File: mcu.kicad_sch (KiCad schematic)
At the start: 12 parts, among them U1 STM32G071C8Tx, Y1 NX3215SA-32.768K-STD-MUA-9

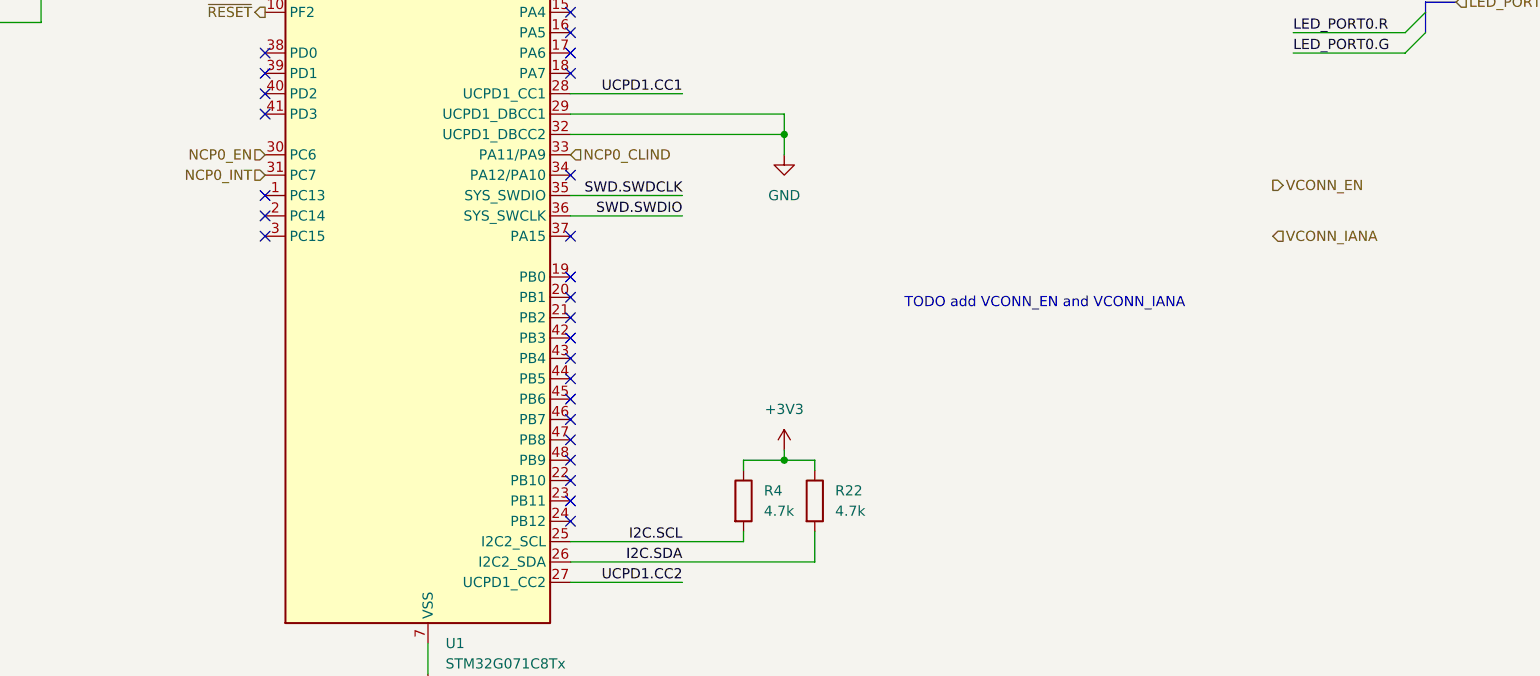
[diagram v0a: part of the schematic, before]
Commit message: Wire up vconn and analog pins
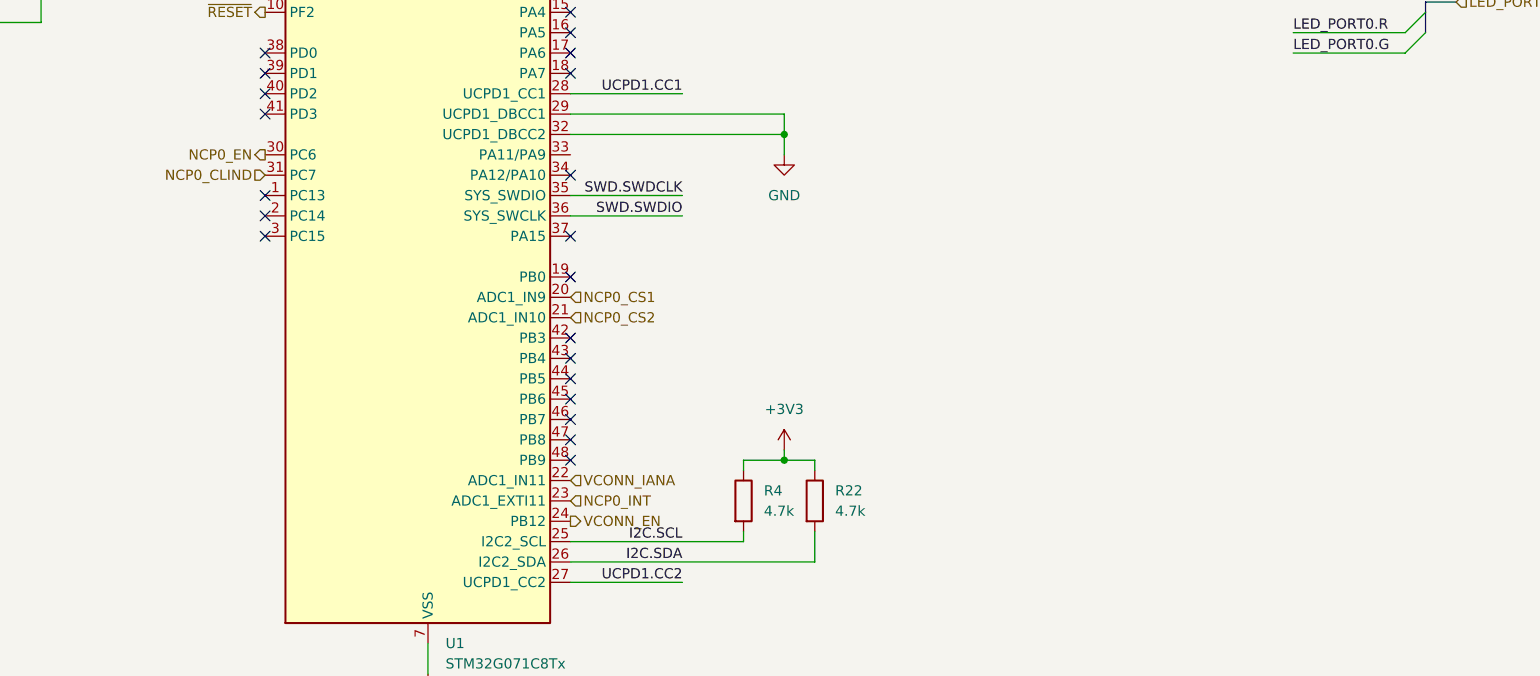
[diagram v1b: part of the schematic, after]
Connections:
- net NCP0_CLIND: now also U1.31 (PC7); no longer U1.33 (PA11/PA9)
- net NCP0_INT: now also U1.23 (PB11); no longer U1.31 (PC7)
- net VCONN_EN: now also U1.24 (PB12)
- net VCONN_IANA: now also U1.22 (PB10)
- net NCP0_CS1: now reaches U1.20 (PB1)
- net NCP0_CS2: now reaches U1.21 (PB2)
- no-connect marks 28 -> 23
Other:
- note removed: "TODO add VCONN_EN and VCONN_IANA"
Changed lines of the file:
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@@
-	)
-	(no_connect
-		(at 149.86 140.97)
-	)
-	(no_connect
-		(at 149.86 115.57)
 	)
 	(no_connect
@@
 	)
 	(no_connect
-		(at 149.86 138.43)
-	)
-	(no_connect
 		(at 149.86 74.93)
 	)
@@
 	)
 	(no_connect
-		(at 149.86 135.89)
-	)
-	(no_connect
 		(at 149.86 130.81)
 	)
@@
 	(no_connect
 		(at 149.86 105.41)
-	)
-	(no_connect
-		(at 149.86 113.03)
 	)
 	(bus_entry
@@
 		)
 	)
-	(text "TODO add VCONN_EN and VCONN_IANA"
-		(exclude_from_sim no)
-		(at 209.042 113.792 0)
-		(effects
-			(font
-				(size 1.27 1.27)
-			)
-		)
-	)
 	(text "- USB PD primer (TI): https://www.ti.com/lit/wp/slyy109b/slyy109b.pdf?ts=1711082549009\n"
 		(exclude_from_sim no)
@@
 	(hierarchical_label "VCONN_EN"
 		(shape output)
-		(at 237.49 99.06 0)
+		(at 149.86 140.97 0)
 		(fields_autoplaced yes)
 		(effects
@@
 	(hierarchical_label "NCP0_CLIND"
 		(shape input)
-		(at 149.86 95.25 0)
+		(at 111.76 97.79 180)
+		(fields_autoplaced yes)
+		(effects
+			(font
+				(size 1.27 1.27)
+			)
+			(justify right)
+		)
+	)
+	(hierarchical_label "NCP0_EN"
+		(shape output)
+		(at 111.76 95.25 180)
+		(fields_autoplaced yes)
+		(effects
+			(font
+				(size 1.27 1.27)
+			)
+			(justify right)
+		)
+	)
+	(hierarchical_label "NCP0_CS2"
+		(shape input)
+		(at 149.86 115.57 0)
 		(fields_autoplaced yes)
 		(effects
@@
 		)
 	)
-	(hierarchical_label "NCP0_EN"
+	(hierarchical_label "NCP0_CS1"
 		(shape input)
-		(at 111.76 95.25 180)
-		(fields_autoplaced yes)
-		(effects
-			(font
-				(size 1.27 1.27)
-			)
-			(justify right)
+		(at 149.86 113.03 0)
+		(fields_autoplaced yes)
+		(effects
+			(font
+				(size 1.27 1.27)
+			)
+			(justify left)
 		)
 	)
@@
 	(hierarchical_label "NCP0_INT"
 		(shape input)
-		(at 111.76 97.79 180)
-		(fields_autoplaced yes)
-		(effects
-			(font
-				(size 1.27 1.27)
-			)
-			(justify right)
+		(at 149.86 138.43 0)
+		(fields_autoplaced yes)
+		(effects
+			(font
+				(size 1.27 1.27)
+			)
+			(justify left)
 		)
 	)
 	(hierarchical_label "VCONN_IANA"
 		(shape input)
-		(at 237.49 105.41 0)
+		(at 149.86 135.89 0)
 		(fields_autoplaced yes)
 		(effects
@@
 		)
 		(pin "21"
+			(alternate "ADC1_IN10")
 		)
 		(pin "10"
@@
 		)
 		(pin "23"
+			(alternate "ADC1_EXTI11")
 		)
 		(pin "45"
@@
 		)
 		(pin "20"
+			(alternate "ADC1_IN9")
 		)
 		(pin "19"
 		)
 		(pin "22"
+			(alternate "ADC1_IN11")
 		)
 		(pin "33"
@@
 		)
 		(pin "24"
+			(alternate "PB12")
 		)
 		(pin "36"

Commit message: Wire up VCONN_FLGn
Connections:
- net NCP0_INT: now also U1.33 (PA11/PA9); no longer U1.23 (PB11)
- new net VCONN_FLGn: U1.23 (PB11)
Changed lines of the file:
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@@
+		)
+	)
+	(hierarchical_label "VCONN_FLGn"
+		(shape input)
+		(at 149.86 138.43 0)
+		(fields_autoplaced yes)
+		(effects
+			(font
+				(size 1.27 1.27)
+			)
+			(justify left)
 		)
 	)
@@
 	(hierarchical_label "NCP0_INT"
 		(shape input)
-		(at 149.86 138.43 0)
+		(at 149.86 95.25 0)
 		(fields_autoplaced yes)
 		(effects

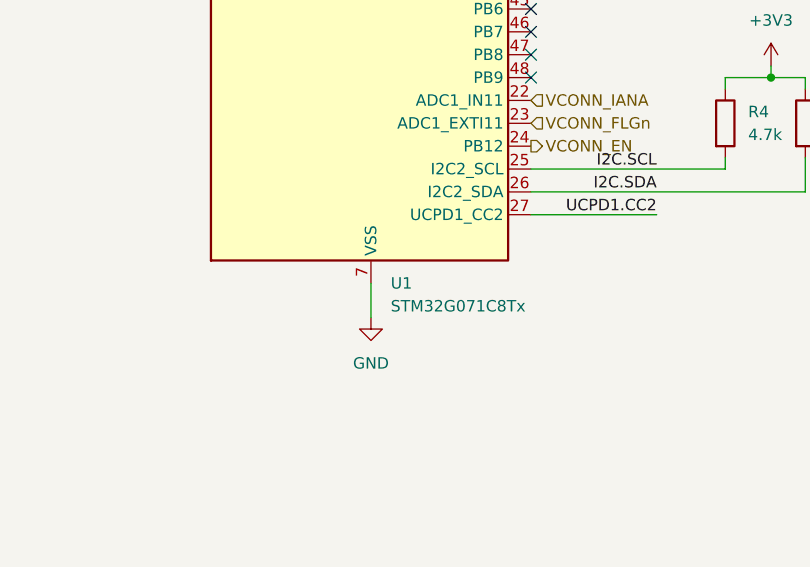
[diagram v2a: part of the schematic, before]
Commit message: Fix ERC errors, swap out mosfets for NVC chip
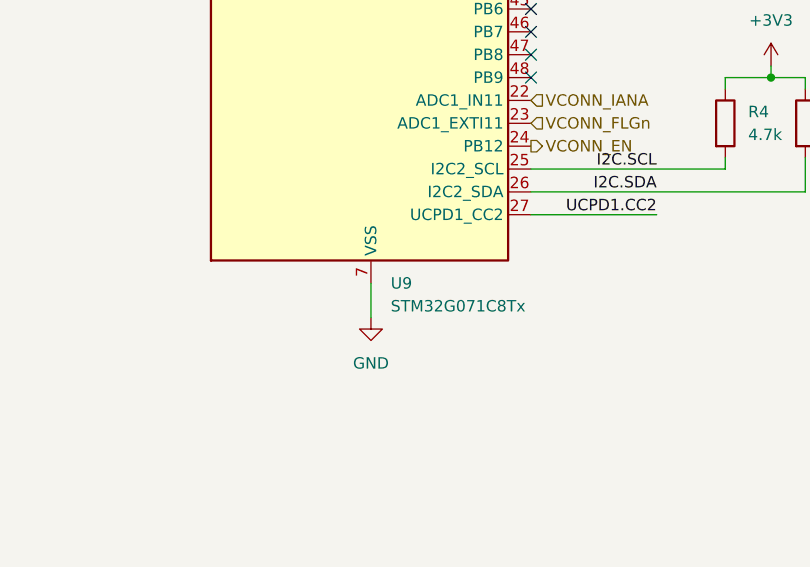
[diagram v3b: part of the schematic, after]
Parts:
- removed U1: STM32G071C8Tx, Package_QFP:LQFP-48_7x7mm_P0.5mm, symbol MCU_ST_STM32G0:STM32G071C8Tx
- added U9: STM32G071C8Tx, Package_QFP:LQFP-48_7x7mm_P0.5mm, symbol MCU_ST_STM32G0:STM32G071C8Tx
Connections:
- net +3V3: now also U9.4 (VBAT), U9.5 (VREF+), U9.6 (VDD)
- net GND: now also U9.29 (PA9/UCPD1_DBCC1), U9.32 (PA10/UCPD1_DBCC2), U9.7 (VSS)
- net I2C.SCL: now also U9.25 (PB13)
- net I2C.SDA: now also U9.26 (PB14)
- net LED_PORT0.G: now also U9.13 (PA2)
- net LED_PORT0.R: now also U9.12 (PA1)
- net NCP0_CLIND: now also U9.31 (PC7)
- net NCP0_CS1: now also U9.20 (PB1)
- net NCP0_CS2: now also U9.21 (PB2)
- net NCP0_EN: now also U9.30 (PC6)
- net NCP0_INT: now also U9.33 (PA11/PA9)
- net SWD.SWDCLK: now also U9.35 (PA13)
- net SWD.SWDIO: now also U9.36 (PA14)
- net UCPD1.CC1: now also U9.28 (PA8)
- net UCPD1.CC2: now also U9.27 (PB15)
- net VCONN_EN: now also U9.24 (PB12)
- net VCONN_FLGn: now also U9.23 (PB11)
- net VCONN_IANA: now also U9.22 (PB10)
- net ~{RESET}: now also U9.10 (PF2)
- net at C29.2, Y1.2: now also U9.8 (PF0)
- net at C30.2, Y1.1: now also U9.9 (PF1)
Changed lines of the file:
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@@
+	)
+	(symbol
+		(lib_name "STM32G071C8Tx_1")
+		(lib_id "MCU_ST_STM32G0:STM32G071C8Tx")
+		(at 129.54 110.49 0)
+		(unit 1)
+		(exclude_from_sim no)
+		(in_bom yes)
+		(on_board yes)
+		(dnp no)
+		(fields_autoplaced yes)
+		(property "Reference" "U9"
+			(at 134.2741 156.21 0)
+			(effects
+				(font
+					(size 1.27 1.27)
+				)
+				(justify left)
+			)
+		)
+		(property "Value" "STM32G071C8Tx"
+			(at 134.2741 158.75 0)
+			(effects
+				(font
+					(size 1.27 1.27)
+				)
+				(justify left)
+			)
+		)
+		(property "Footprint" "Package_QFP:LQFP-48_7x7mm_P0.5mm"
+			(at 114.3 153.67 0)
+			(effects
+				(font
+					(size 1.27 1.27)
+				)
+				(justify right)
+				(hide yes)
+			)
+		)
+		(property "Datasheet" "https://www.st.com/resource/en/datasheet/stm32g071c8.pdf"
+			(at 129.54 110.49 0)
+			(effects
+				(font
+					(size 1.27 1.27)
+				)
+				(hide yes)
+			)
+		)
+		(property "Description" "STMicroelectronics Arm Cortex-M0+ MCU, 64KB flash, 36KB RAM, 64 MHz, 1.7-3.6V, 44 GPIO, LQFP48"
+			(at 129.54 110.49 0)
+			(effects
+				(font
+					(size 1.27 1.27)
+				)
+				(hide yes)
+			)
+		)
+		(pin "6"
+		)
+		(pin "21"
+			(alternate "ADC1_IN10")
+		)
+		(pin "5"
+		)
+		(pin "37"
+		)
+		(pin "36"
+			(alternate "SYS_SWCLK")
+		)
+		(pin "29"
+			(alternate "UCPD1_DBCC1")
+		)
+		(pin "22"
+			(alternate "ADC1_IN11")
+		)
+		(pin "30"
+		)
+		(pin "15"
+		)
+		(pin "48"
+		)
+		(pin "43"
+		)
+		(pin "18"
+		)
+		(pin "45"
+		)
+		(pin "44"
+		)
+		(pin "4"
+		)
+		(pin "11"
+		)
+		(pin "19"
+		)
+		(pin "13"
+			(alternate "TIM2_CH3")
+		)
+		(pin "7"
+		)
+		(pin "3"
+		)
+		(pin "46"
+		)
+		(pin "33"
+		)
+		(pin "24"
+		)
+		(pin "31"
+		)
+		(pin "41"
+		)
+		(pin "27"
+			(alternate "UCPD1_CC2")
+		)
+		(pin "17"
+		)
+		(pin "32"
+			(alternate "UCPD1_DBCC2")
+		)
+		(pin "40"
+		)
+		(pin "23"
+			(alternate "ADC1_EXTI11")
+		)
+		(pin "9"
+			(alternate "RCC_OSC_OUT")
+		)
+		(pin "35"
+			(alternate "SYS_SWDIO")
+		)
+		(pin "28"
+			(alternate "UCPD1_CC1")
+		)
+		(pin "39"
+		)
+		(pin "38"
+		)
+		(pin "25"
+			(alternate "I2C2_SCL")
+		)
+		(pin "20"
+			(alternate "ADC1_IN9")
+		)
+		(pin "2"
+		)
+		(pin "34"
+		)
+		(pin "42"
+		)
+		(pin "47"
+		)
+		(pin "16"
+		)
+		(pin "12"
+			(alternate "TIM2_CH2")
+		)
+		(pin "14"
+			(alternate "TIM2_CH4")
+		)
+		(pin "26"
+			(alternate "I2C2_SDA")
+		)
+		(pin "8"
+			(alternate "RCC_OSC_IN")
+		)
+		(pin "1"
+		)
+		(pin "10"
+		)
+		(instances
+			(project ""
+				(path "/1eef11ed-4055-4fe6-b7fc-0d497914d6cc/c7a7dbb8-992c-4c2f-932e-320edf489341"
+					(reference "U9")
+					(unit 1)
+				)
+			)
+		)
 	)
 	(symbol
@@
 					(unit 1)
 				)
-			)
-		)
-	)
-	(symbol
-		(lib_id "MCU_ST_STM32G0:STM32G071C8Tx")
-		(at 129.54 110.49 0)
-		(unit 1)
-		(exclude_from_sim no)
-		(in_bom yes)
-		(on_board yes)
-		(dnp no)
-		(fields_autoplaced yes)
-		(property "Reference" "U1"
-			(at 134.2741 156.21 0)
-			(effects
-				(font
-					(size 1.27 1.27)
-				)
-				(justify left)
-			)
-		)
-		(property "Value" "STM32G071C8Tx"
-			(at 134.2741 158.75 0)
-			(effects
-				(font
-					(size 1.27 1.27)
-				)
-				(justify left)
-			)
-		)
-		(property "Footprint" "Package_QFP:LQFP-48_7x7mm_P0.5mm"
-			(at 114.3 153.67 0)
-			(effects
-				(font
-					(size 1.27 1.27)
-				)
-				(justify right)
-				(hide yes)
-			)
-		)
-		(property "Datasheet" "https://www.st.com/resource/en/datasheet/stm32g071c8.pdf"
-			(at 129.54 110.49 0)
-			(effects
-				(font
-					(size 1.27 1.27)
-				)
-				(hide yes)
-			)
-		)
-		(property "Description" ""
-			(at 129.54 110.49 0)
-			(effects
-				(font
-					(size 1.27 1.27)
-				)
-				(hide yes)
-			)
-		)
-		(property "LCSC Part No" ""
-			(at 129.54 110.49 0)
-			(effects
-				(font
-					(size 1.27 1.27)
-				)
-				(hide yes)
-			)
-		)
-		(property "JLCPCB Part No" "C529341"
-			(at 129.54 110.49 0)
-			(effects
-				(font
-					(size 1.27 1.27)
-				)
-				(hide yes)
-			)
-		)
-		(property "V_{max}" ""
-			(at 129.54 110.49 0)
-			(effects
-				(font
-					(size 1.27 1.27)
-				)
-			)
-		)
-		(pin "37"
-		)
-		(pin "21"
-			(alternate "ADC1_IN10")
-		)
-		(pin "10"
-		)
-		(pin "7"
-		)
-		(pin "3"
-		)
-		(pin "2"
-		)
-		(pin "18"
-		)
-		(pin "4"
-		)
-		(pin "5"
-		)
-		(pin "23"
-			(alternate "ADC1_EXTI11")
-		)
-		(pin "45"
-		)
-		(pin "17"
-		)
-		(pin "35"
-			(alternate "SYS_SWDIO")
-		)
-		(pin "15"
-		)
-		(pin "48"
-		)
-		(pin "14"
-			(alternate "TIM2_CH4")
-		)
-		(pin "20"
-			(alternate "ADC1_IN9")
-		)
-		(pin "19"
-		)
-		(pin "22"
-			(alternate "ADC1_IN11")
-		)
-		(pin "33"
-		)
-		(pin "27"
-			(alternate "UCPD1_CC2")
-		)
-		(pin "13"
-			(alternate "TIM2_CH3")
-		)
-		(pin "28"
-			(alternate "UCPD1_CC1")
-		)
-		(pin "29"
-			(alternate "UCPD1_DBCC1")
-		)
-		(pin "40"
-		)
-		(pin "26"
-			(alternate "I2C2_SDA")
-		)
-		(pin "38"
-		)
-		(pin "31"
-		)
-		(pin "9"
-			(alternate "RCC_OSC_OUT")
-		)
-		(pin "30"
-		)
-		(pin "39"
-		)
-		(pin "34"
-		)
-		(pin "44"
-		)
-		(pin "47"
-		)
-		(pin "41"
-		)
-		(pin "42"
-		)
-		(pin "46"
-		)
-		(pin "24"
-			(alternate "PB12")
-		)
-		(pin "36"
-			(alternate "SYS_SWCLK")
-		)
-		(pin "8"
-			(alternate "RCC_OSC_IN")
-		)
-		(pin "32"
-			(alternate "UCPD1_DBCC2")
-		)
-		(pin "1"
-		)
-		(pin "16"
-		)
-		(pin "25"
-			(alternate "I2C2_SCL")
-		)
-		(pin "11"
-		)
-		(pin "43"
-		)
-		(pin "6"
-		)
-		(pin "12"
-			(alternate "TIM2_CH2")
-		)
-		(instances
-			(project "usb-zekers"
-				(path "/1eef11ed-4055-4fe6-b7fc-0d497914d6cc/c7a7dbb8-992c-4c2f-932e-320edf489341"
-					(reference "U1")
-					(unit 1)
-				)

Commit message: more footprints
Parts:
- C21: footprint (none) -> Capacitor_SMD:C_0603_1608Metric; JLCPCB Part No (none) -> C19666
- C22, C24: footprint (none) -> Capacitor_SMD:C_0603_1608Metric
- C23: footprint (none) -> Capacitor_SMD:C_0402_1005Metric; JLCPCB Part No (none) -> C52923
- R22, R4: footprint (none) -> Resistor_SMD:R_1206_3216Metric; JLCPCB Part No (none) -> C17936
- TP1, TP2: footprint (none) -> TestPoint:TestPoint_Pad_D1.0mm
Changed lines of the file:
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@@
 			)
 		)
-		(property "Footprint" ""
+		(property "Footprint" "Capacitor_SMD:C_0603_1608Metric"
 			(at 70.8152 176.53 0)
 			(effects
@@
 			)
 		)
-		(property "Footprint" ""
+		(property "Footprint" "Capacitor_SMD:C_0603_1608Metric"
 			(at 46.6852 176.53 0)
 			(effects
@@
 			)
 		)
-		(property "Footprint" ""
+		(property "Footprint" "Resistor_SMD:R_1206_3216Metric"
 			(at 178.562 138.43 90)
 			(effects
@@
 			)
 		)
-		(property "JLCPCB Part No" ""
+		(property "JLCPCB Part No" "C17936"
 			(at 180.34 138.43 0)
 			(effects
@@
 			)
 		)
-		(property "Footprint" ""
+		(property "Footprint" "Capacitor_SMD:C_0402_1005Metric"
 			(at 59.3852 176.53 0)
 			(effects
@@
 			)
 		)
-		(property "JLCPCB Part No" ""
+		(property "JLCPCB Part No" "C52923"
 			(at 58.42 172.72 0)
 			(effects
@@
 			)
 		)
-		(property "Footprint" ""
+		(property "Footprint" "TestPoint:TestPoint_Pad_D1.0mm"
 			(at 231.14 34.29 0)
 			(effects
@@
 			)
 		)
-		(property "Footprint" ""
+		(property "Footprint" "TestPoint:TestPoint_Pad_D1.0mm"
 			(at 231.14 31.75 0)
 			(effects
@@
 			)
 		)
-		(property "Footprint" ""
+		(property "Footprint" "Resistor_SMD:R_1206_3216Metric"
 			(at 169.672 138.43 90)
 			(effects
@@
 			)
 		)
-		(property "JLCPCB Part No" ""
+		(property "JLCPCB Part No" "C17936"
 			(at 171.45 138.43 0)
 			(effects
@@
 			)
 		)
-		(property "Footprint" ""
+		(property "Footprint" "Capacitor_SMD:C_0603_1608Metric"
 			(at 33.9852 176.53 0)
 			(effects
@@
 			)
 		)
-		(property "JLCPCB Part No" ""
+		(property "JLCPCB Part No" "C19666"
 			(at 33.02 172.72 0)
 			(effects
